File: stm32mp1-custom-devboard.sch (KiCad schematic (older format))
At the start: 1 part, among them P1 Main Power Supply

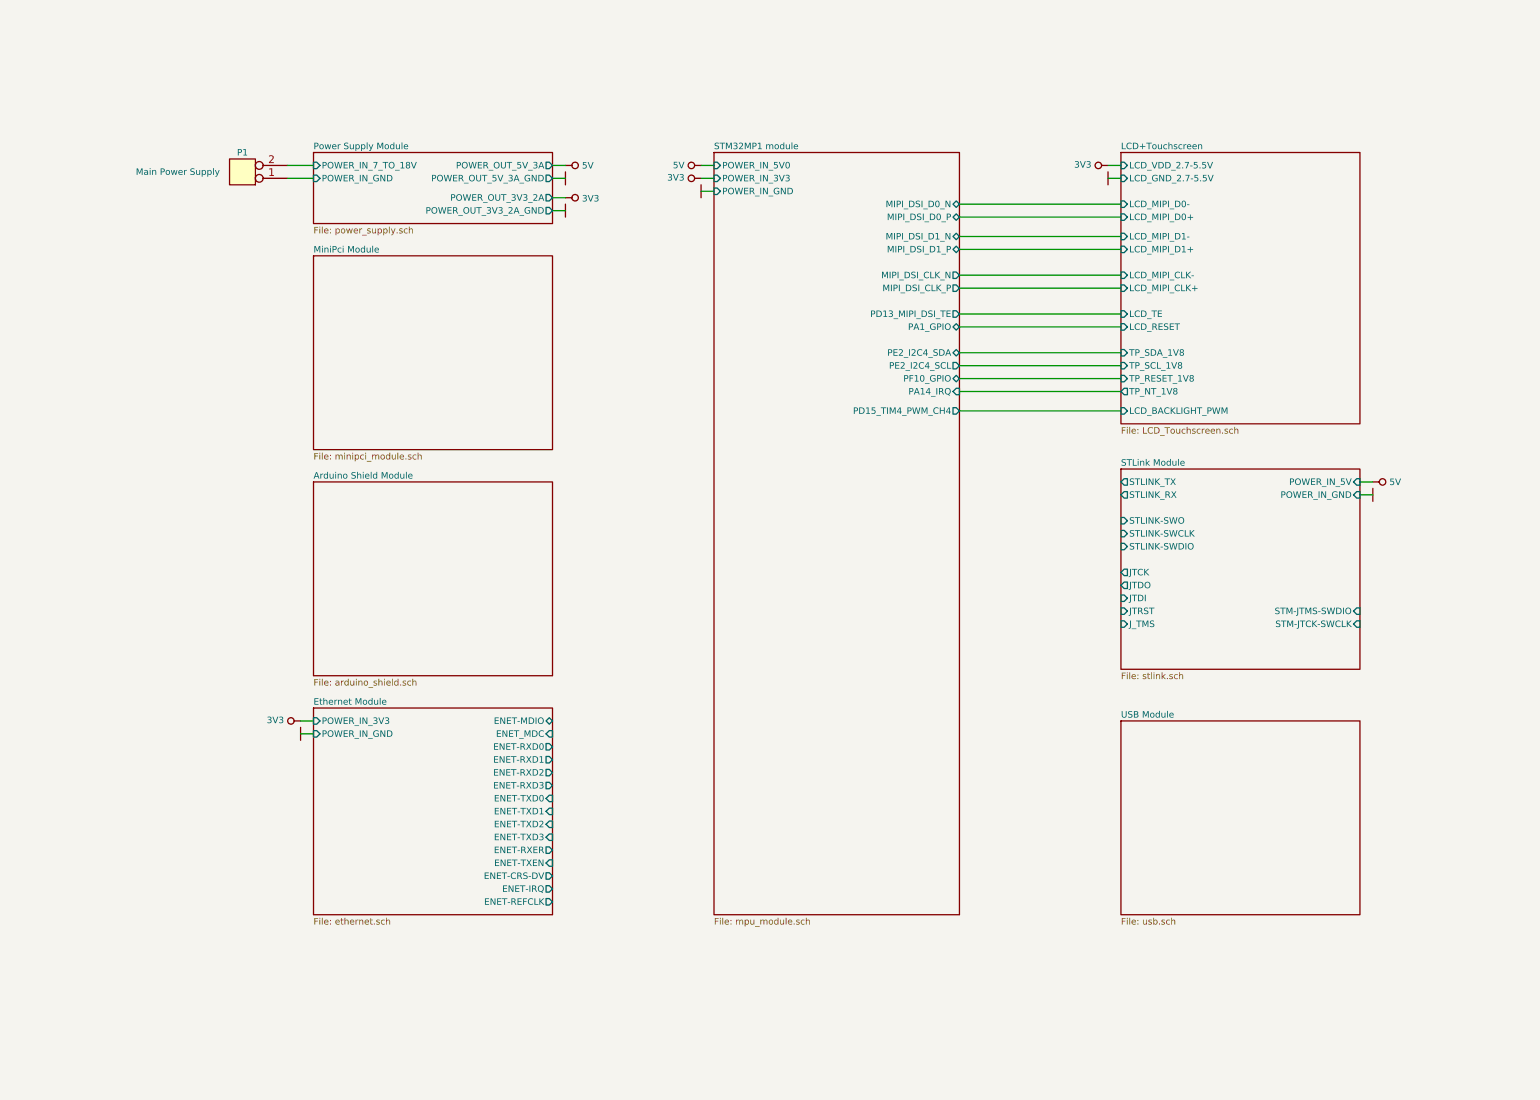
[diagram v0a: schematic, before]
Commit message: Updated schematic, added some components, figurated components on pcb
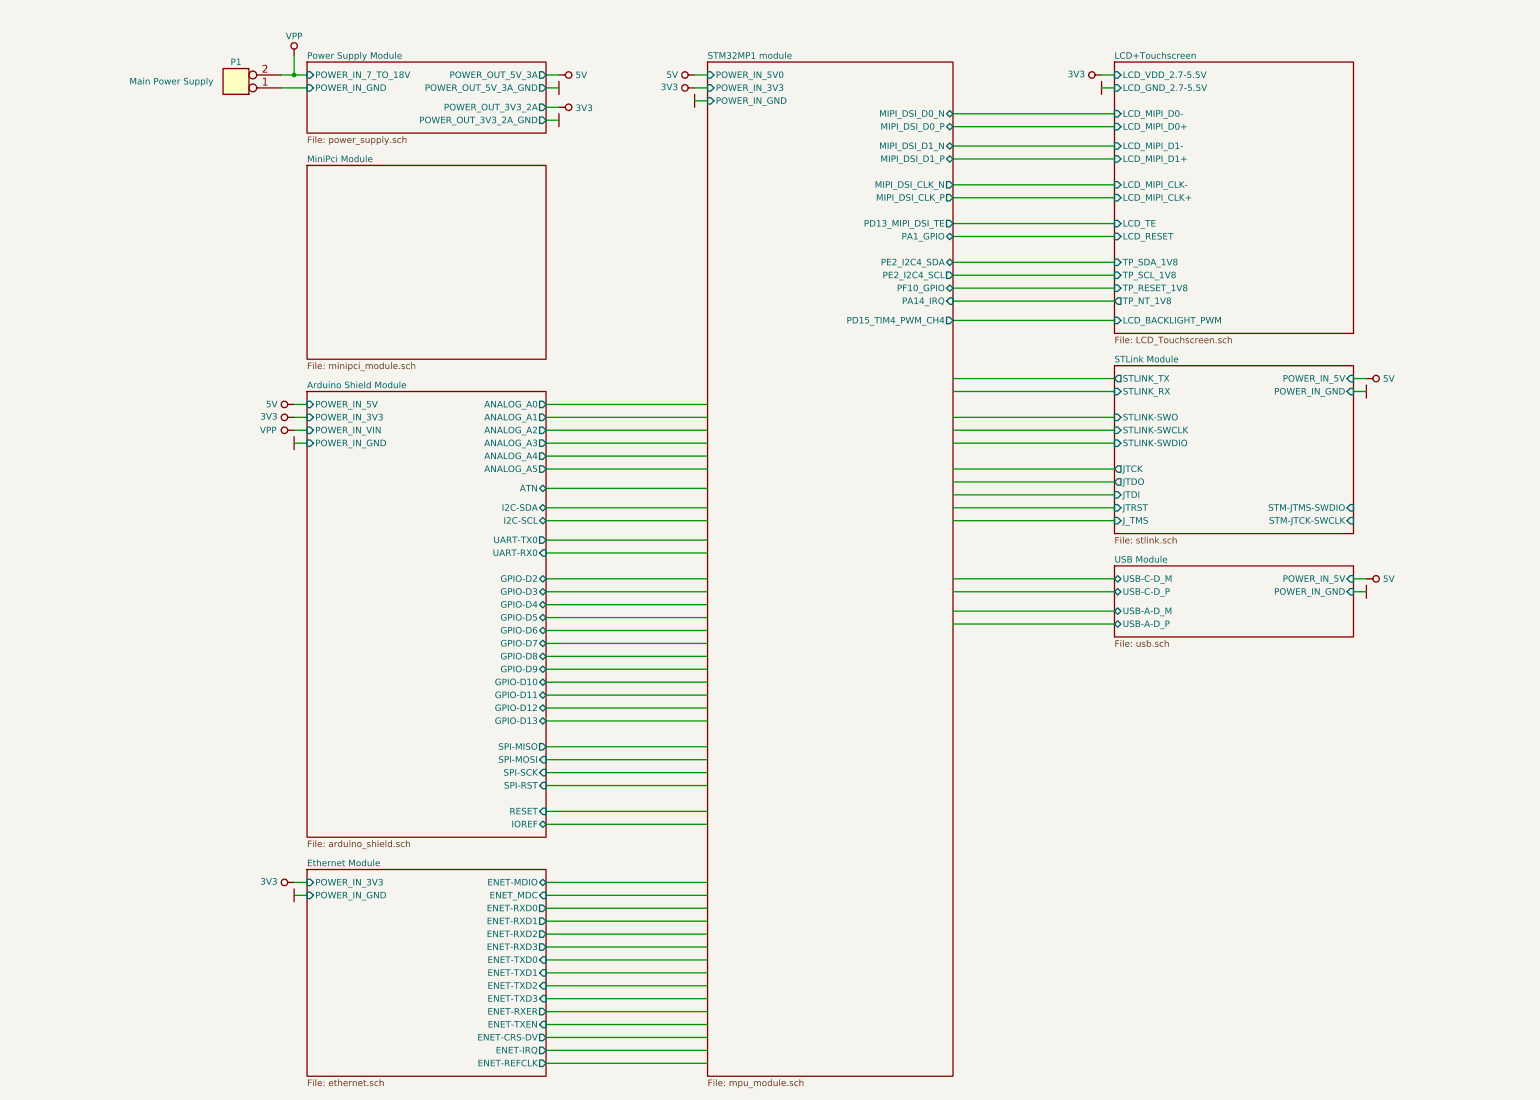
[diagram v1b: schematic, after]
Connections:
- net labels added: VPP
- wire segments 28 -> 94
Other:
- moved on the sheet: P1

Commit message: Schematic work contiune, added pinout spreadsheet
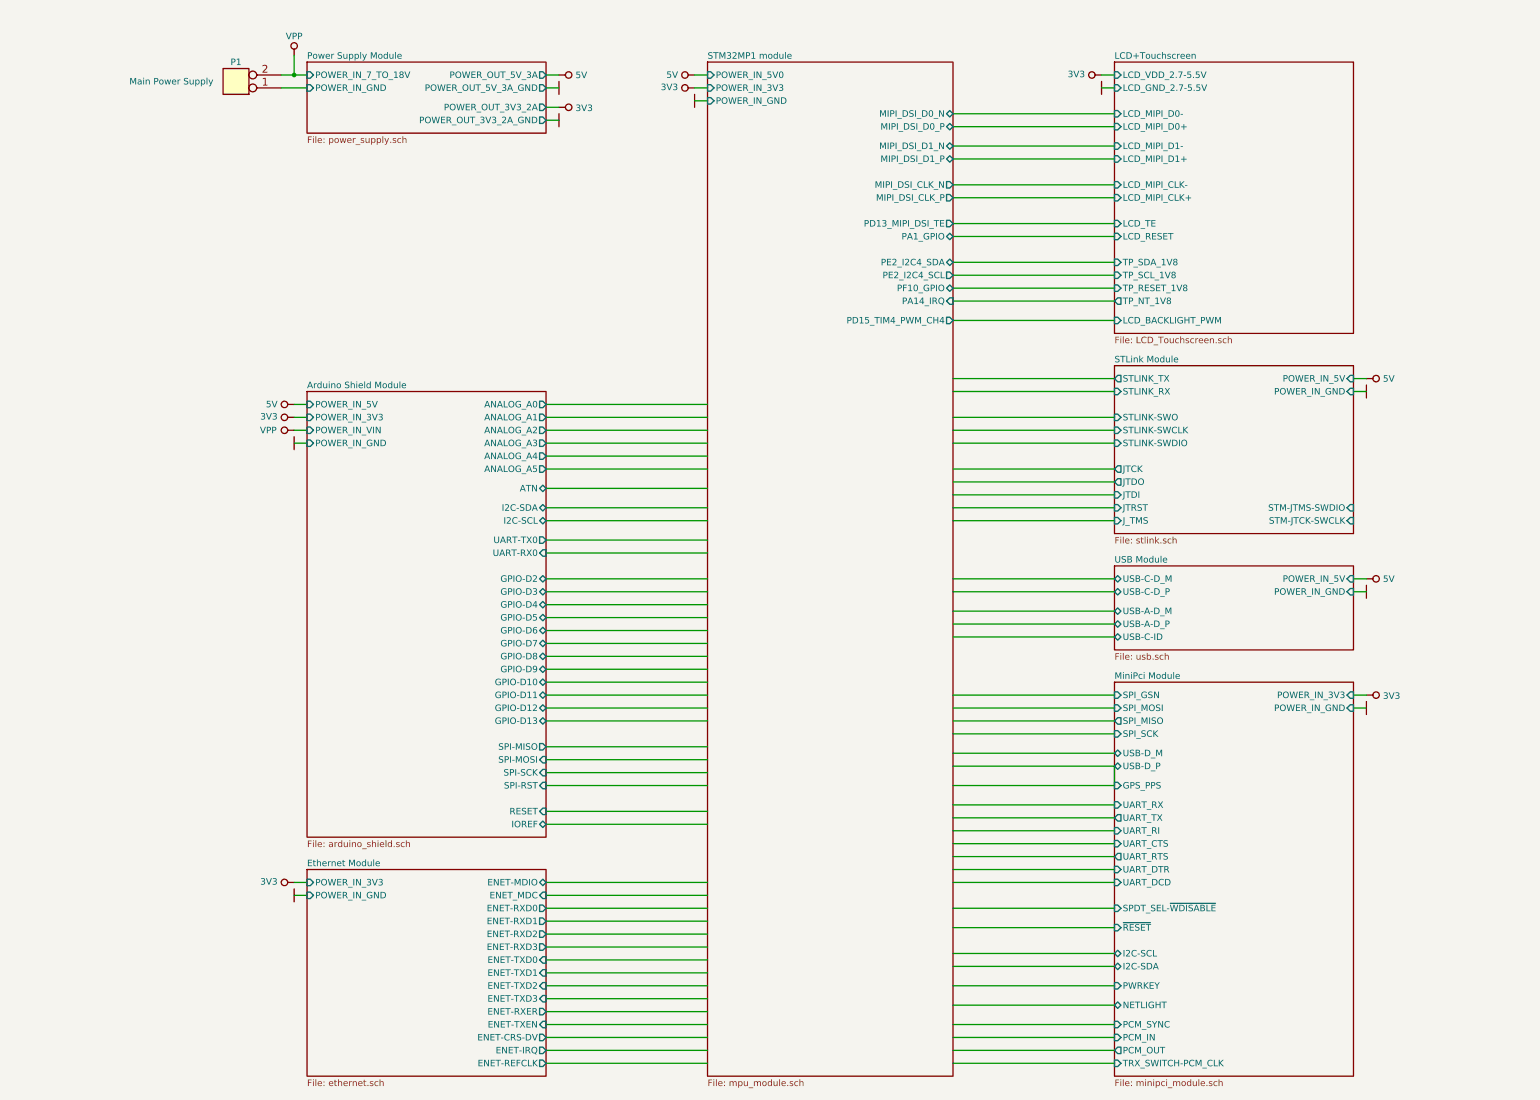
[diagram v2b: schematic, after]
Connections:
- wire segments 94 -> 122
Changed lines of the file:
@@
 $EndSheet
 $Sheet
-S 4400 2400 1850 1500
+S 10650 6400 1850 3050
 U 5FFEC95A
 F0 "MiniPci Module" 50
 F1 "minipci_module.sch" 50
+F2 "TRX_SWITCH-PCM_CLK" I L 10650 9350 50
+F3 "GPS_PPS" I L 10650 7200 50
+F4 "SPI_GSN" I L 10650 6500 50
+F5 "SPI_MOSI" I L 10650 6600 50
+F6 "SPI_SCK" I L 10650 6800 50
+F7 "SPDT_SEL-~WDISABLE~" I L 10650 8150 50
+F8 "USB-D_M" B L 10650 6950 50
+F9 "USB-D_P" B L 10650 7050 50
+F10 "PWRKEY" I L 10650 8750 50
+F11 "UART_RX" I L 10650 7350 50
+F12 "UART_RI" I L 10650 7550 50
+F13 "UART_CTS" I L 10650 7650 50
+F14 "UART_DTR" I L 10650 7850 50
+F15 "UART_DCD" I L 10650 7950 50
+F16 "~RESET~" I L 10650 8300 50
+F17 "I2C-SCL" B L 10650 8500 50
+F18 "I2C-SDA" B L 10650 8600 50
+F19 "NETLIGHT" B L 10650 8900 50
+F20 "PCM_SYNC" I L 10650 9050 50
+F21 "PCM_IN" I L 10650 9150 50
+F22 "POWER_IN_GND" I R 12500 6600 50
+F23 "POWER_IN_3V3" I R 12500 6500 50
+F24 "UART_TX" O L 10650 7450 50
+F25 "UART_RTS" O L 10650 7750 50
+F26 "PCM_OUT" O L 10650 9250 50
+F27 "SPI_MISO" O L 10650 6700 50
 $EndSheet
 $Sheet
@@
 	4300 7950 4400 7950
 $Sheet
-S 10650 5500 1850 550
+S 10650 5500 1850 650
 U 60014762
 F0 "USB Module" 50
@@
 F6 "USB-A-D_M" B L 10650 5850 50
 F7 "USB-A-D_P" B L 10650 5950 50
+F8 "USB-C-ID" B L 10650 6050 50
 $EndSheet
 $Comp
-L power:5V #PWR?
+L power:5V #PWR0164
 U 1 1 601CC4D8
 P 12600 5600
-F 0 "#PWR?" V 12550 5600 20  0001 C CNN
+F 0 "#PWR0164" V 12550 5600 20  0001 C CNN
 F 1 "5V" V 12601 5728 50  0000 L CNN
 F 2 "" H 12600 5600 60  0000 C CNN
@@
 	12500 5600 12600 5600
 $Comp
-L power:GND #PWR?
+L power:GND #PWR0165
 U 1 1 601CC5A7
 P 12600 5700
-F 0 "#PWR?" H 12600 5800 30  0001 C CNN
+F 0 "#PWR0165" H 12600 5800 30  0001 C CNN
 F 1 "GND" H 12600 5600 30  0001 C CNN
 F 2 "" H 12600 5700 60  0000 C CNN
@@
 	12500 5700 12600 5700
 $Comp
-L power:5V #PWR?
+L power:5V #PWR0166
 U 1 1 601CEF0D
 P 4300 4250
-F 0 "#PWR?" V 4250 4250 20  0001 C CNN
+F 0 "#PWR0166" V 4250 4250 20  0001 C CNN
 F 1 "5V" V 4301 4378 50  0000 L CNN
 F 2 "" H 4300 4250 60  0000 C CNN
@@
 	4400 4250 4300 4250
 $Comp
-L power:GND #PWR?
+L power:GND #PWR0167
 U 1 1 601CEFF6
 P 4300 4550
-F 0 "#PWR?" H 4300 4650 30  0001 C CNN
+F 0 "#PWR0167" H 4300 4650 30  0001 C CNN
 F 1 "GND" H 4300 4450 30  0001 C CNN
 F 2 "" H 4300 4550 60  0000 C CNN
@@
 	4400 4550 4300 4550
 $Comp
-L power:3V3 #PWR?
+L power:3V3 #PWR0168
 U 1 1 601D3B80
 P 4300 4350
-F 0 "#PWR?" H 4300 4450 40  0001 C CNN
+F 0 "#PWR0168" H 4300 4450 40  0001 C CNN
 F 1 "3V3" V 4306 4478 50  0000 L CNN
 F 2 "" H 4300 4350 60  0000 C CNN
@@
 	4300 1700 4400 1700
 $Comp
-L power:VPP #PWR?
+L power:VPP #PWR0169
 U 1 1 601DBB64
 P 4300 1550
-F 0 "#PWR?" H 4300 1750 40  0001 C CNN
+F 0 "#PWR0169" H 4300 1750 40  0001 C CNN
 F 1 "VPP" H 4300 1700 50  0000 C CNN
 F 2 "" H 4300 1550 60  0000 C CNN
@@
 $EndComp
 $Comp
-L power:VPP #PWR?
+L power:VPP #PWR0170
 U 1 1 601DEBB6
 P 4300 4450
-F 0 "#PWR?" H 4300 4650 40  0001 C CNN
+F 0 "#PWR0170" H 4300 4650 40  0001 C CNN
 F 1 "VPP" V 4300 4650 50  0000 C CNN
 F 2 "" H 4300 4450 60  0000 C CNN
@@
 Wire Wire Line
 	6250 4250 7500 4250
+Wire Wire Line
+	10650 6050 9400 6050
+$Comp
+L power:GND #PWR?
+U 1 1 601608A8
+P 12600 6600
+F 0 "#PWR?" H 12600 6700 30  0001 C CNN
+F 1 "GND" H 12600 6500 30  0001 C CNN
+F 2 "" H 12600 6600 60  0000 C CNN
+F 3 "" H 12600 6600 60  0000 C CNN
+	1    12600 6600
+	0    1    1    0
+$EndComp
+$Comp
+L power:3V3 #PWR?
+U 1 1 601609D2
+P 12600 6500
+F 0 "#PWR?" H 12600 6600 40  0001 C CNN
+F 1 "3V3" V 12606 6628 50  0000 L CNN
+F 2 "" H 12600 6500 60  0000 C CNN
+F 3 "" H 12600 6500 60  0000 C CNN
+	1    12600 6500
+	0    1    1    0
+$EndComp
+Wire Wire Line
+	12600 6500 12500 6500
+Wire Wire Line
+	12500 6600 12600 6600
+Wire Wire Line
+	10650 6500 9400 6500
+Wire Wire Line
+	10650 6600 9400 6600
+Wire Wire Line
+	9400 6700 10650 6700
+Wire Wire Line
+	10650 6800 9400 6800
+Wire Wire Line
+	10650 6950 9400 6950
+Wire Wire Line
+	9400 7050 10650 7050
+Wire Wire Line
+	10650 7050 10650 7200
+Wire Wire Line
+	10650 7200 9400 7200
+Wire Wire Line
+	9400 7350 10650 7350
+Wire Wire Line
+	10650 7450 9400 7450
+Wire Wire Line
+	10650 7550 9400 7550
+Wire Wire Line
+	10650 7650 9400 7650
+Wire Wire Line
+	10650 7750 9400 7750
+Wire Wire Line
+	10650 7850 9400 7850
+Wire Wire Line
+	10650 7950 9400 7950
+Wire Wire Line
+	10650 8150 9400 8150
+Wire Wire Line
+	10650 8300 9400 8300
+Wire Wire Line
+	10650 8500 9400 8500
+Wire Wire Line
+	10650 8600 9400 8600
+Wire Wire Line
+	10650 8750 9400 8750
+Wire Wire Line
+	10650 8900 9400 8900
+Wire Wire Line
+	10650 9050 9400 9050
+Wire Wire Line
+	10650 9150 9400 9150
+Wire Wire Line
+	10650 9250 9400 9250
+Wire Wire Line
+	10650 9350 9400 9350
 $EndSCHEMATC

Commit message: Schematic finished, elements figurated on pcb, tracking started
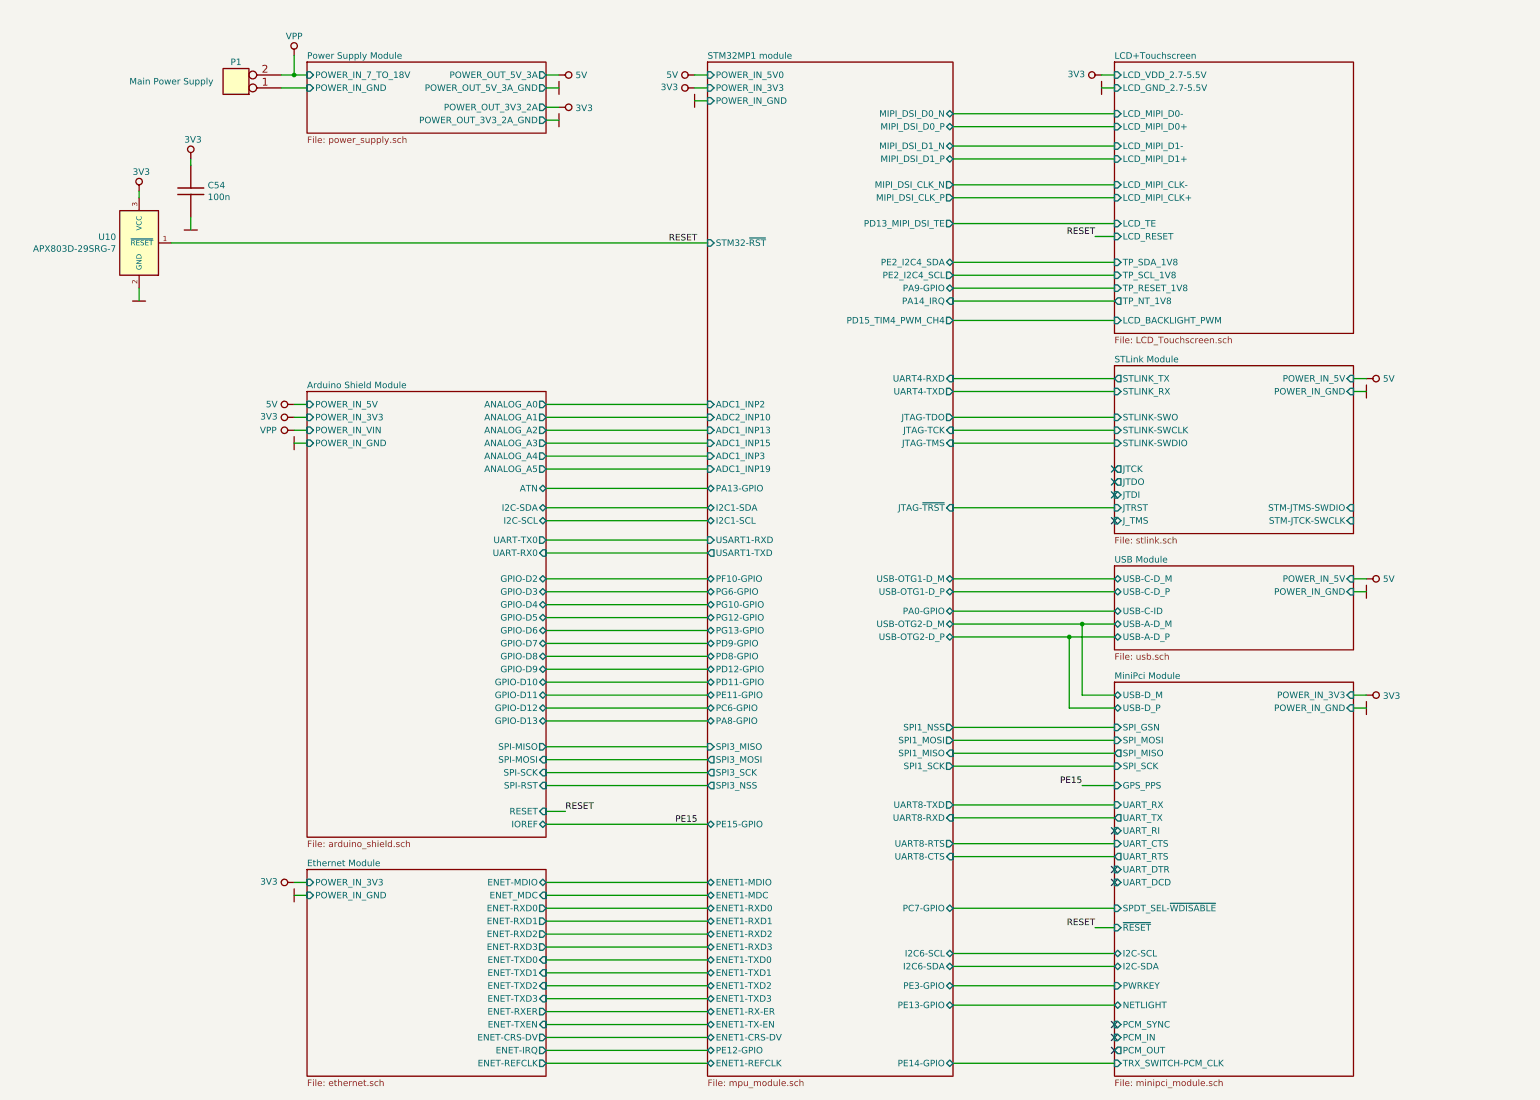
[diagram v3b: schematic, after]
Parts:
- added C54: 100n, Capacitors_Smd_0603:100nF_0603, symbol Capacitors_Smd0603:100n
- added U10: APX803D-29SRG-7, Reset_Device_Diodes:APX803D-29SRG-7, symbol Reset_Devices_Diodes:APX803D-29SRG-7
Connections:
- net labels added: PE15, RESET
- wire segments 122 -> 120
- no-connect marks 0 -> 10

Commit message: Tracking in progress
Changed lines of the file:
@@
 F14 "PA14_IRQ" I R 9400 3450 50
 F15 "PD13_MIPI_DSI_TE" O R 9400 2850 50
-F16 "USB-OTG1-D_M" B R 9400 5600 50
+F16 "USB-OTG1-D_N" B R 9400 5600 50
 F17 "USB-OTG1-D_P" B R 9400 5700 50
-F18 "USB-OTG2-D_M" B R 9400 5950 50
+F18 "USB-OTG2-D_N" B R 9400 5950 50
 F19 "USB-OTG2-D_P" B R 9400 6050 50
 F20 "STM32-~RST~" I L 7500 3000 50
@@
 F2 "POWER_IN_5V" I R 12500 5600 50
 F3 "POWER_IN_GND" I R 12500 5700 50
-F4 "USB-C-D_M" B L 10650 5600 50
+F4 "USB-C-D_N" B L 10650 5600 50
 F5 "USB-C-D_P" B L 10650 5700 50
-F6 "USB-A-D_M" B L 10650 5950 50
+F6 "USB-A-D_N" B L 10650 5950 50
 F7 "USB-A-D_P" B L 10650 6050 50
 F8 "USB-C-ID" B L 10650 5850 50
